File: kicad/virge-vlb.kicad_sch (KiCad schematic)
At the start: 37 parts, among them J2 VGA, U1 86C325, Y1 14.318MHz

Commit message: changed QFP and ROM footprint
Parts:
- J2: footprint Connector_Dsub:DSUB-15-HD_Female_Horizontal_P2.29x1.98mm_EdgePinOffset8.35mm_Housed_MountingHolesOffset10.89mm -> VLB:DSUB-15_female
- U1: footprint Package_QFP:PQFP-208_28x28mm_P0.5mm -> VLB:QFP-208
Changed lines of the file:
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@@
       (effects (font (size 1.524 1.524)) (justify left))
     )
-    (property "Footprint" "Package_QFP:PQFP-208_28x28mm_P0.5mm" (at 201.93 123.19 0)
+    (property "Footprint" "VLB:QFP-208" (at 201.93 123.19 0)
       (effects (font (size 1.524 1.524)) (justify right) hide)
     )
@@
       (effects (font (size 1.27 1.27)))
     )
-    (property "Footprint" "Connector_Dsub:DSUB-15-HD_Female_Horizontal_P2.29x1.98mm_EdgePinOffset8.35mm_Housed_MountingHolesOffset10.89mm" (at 95.25 143.51 0)
+    (property "Footprint" "VLB:DSUB-15_female" (at 95.25 143.51 0)
       (effects (font (size 1.27 1.27)) hide)
     )
@@
       (effects (font (size 1.524 1.524)))
     )
-    (property "Footprint" "Package_QFP:PQFP-208_28x28mm_P0.5mm" (at 149.86 49.53 0)
+    (property "Footprint" "VLB:QFP-208" (at 149.86 49.53 0)
       (effects (font (size 1.524 1.524)) (justify right) hide)
     )

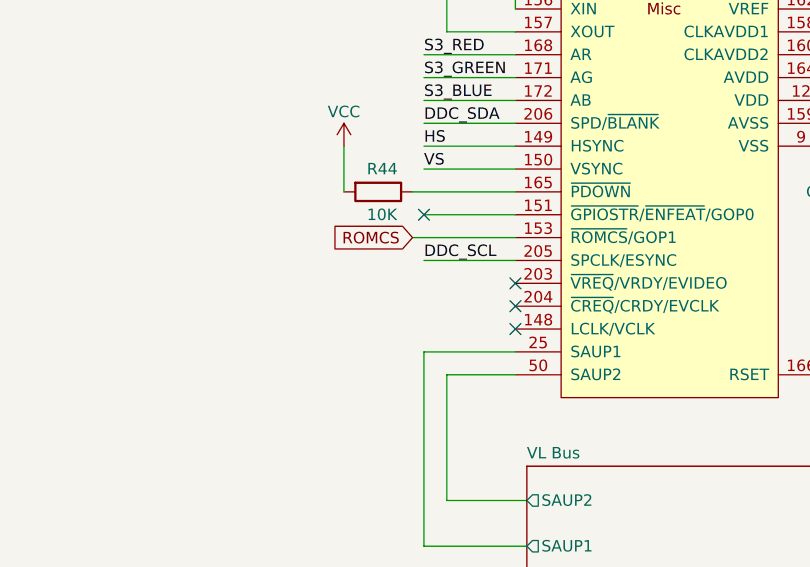
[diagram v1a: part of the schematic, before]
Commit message: added pull up for VREQ
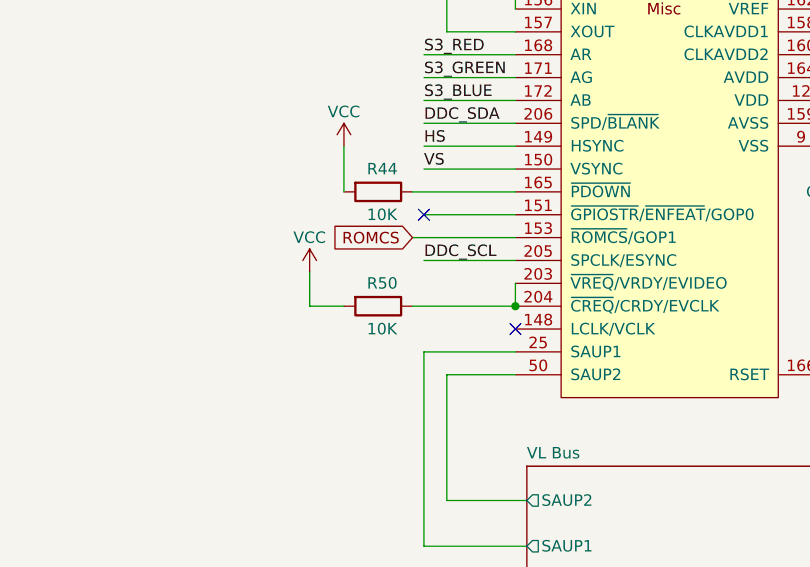
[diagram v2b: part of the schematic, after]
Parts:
- added R50: 10K, Resistor_SMD:R_0805_2012Metric_Pad1.20x1.40mm_HandSolder, symbol Device:R
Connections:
- net VCC: now also R50.2
- net at U1.203 (~{VREQ}/VRDY/EVIDEO): now also U1.204 (~{CREQ}/CRDY/EVCLK), R50.1
- no-connect marks 14 -> 12
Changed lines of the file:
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@@
   (junction (at 219.71 77.47) (diameter 0) (color 0 0 0 0)
+  )
+  (junction (at 173.99 69.85) (diameter 0) (color 0 0 0 0)
   )
   (junction (at 111.76 151.13) (diameter 0) (color 0 0 0 0)
@@
   (no_connect (at 231.14 132.08))
   (no_connect (at 231.14 121.92))
-  (no_connect (at 173.99 69.85))
-  (no_connect (at 173.99 67.31))
   (no_connect (at 231.14 129.54))
   (no_connect (at 63.5 161.29))
@@
     (stroke (width 0) (type default))
   )
+  (wire (pts (xy 173.99 67.31) (xy 173.99 69.85))
+    (stroke (width 0) (type default))
+  )
   (wire (pts (xy 163.83 74.93) (xy 163.83 96.52))
     (stroke (width 0) (type default))
@@
     (stroke (width 0) (type default))
   )
+  (wire (pts (xy 151.13 69.85) (xy 151.13 66.04))
+    (stroke (width 0) (type default))
+  )
   (wire (pts (xy 163.83 44.45) (xy 173.99 44.45))
     (stroke (width 0) (type default))
@@
     (stroke (width 0) (type default))
   )
+  (wire (pts (xy 154.94 69.85) (xy 151.13 69.85))
+    (stroke (width 0) (type default))
+  )
   (wire (pts (xy 111.76 151.13) (xy 111.76 163.83))
     (stroke (width 0) (type default))
@@
   )
   (wire (pts (xy 157.48 27.94) (xy 166.37 27.94))
+    (stroke (width 0) (type default))
+  )
+  (wire (pts (xy 162.56 69.85) (xy 173.99 69.85))
     (stroke (width 0) (type default))
   )
@@
         (path "/e8216711-86b5-4276-82f4-4c7ed22b9a9c"
           (reference "#PWR056") (unit 1)
+        )
+      )
+    )
+  )
+  (symbol (lib_id "power:VCC") (at 151.13 66.04 0) (unit 1)
+    (in_bom yes) (on_board yes) (dnp no) (fields_autoplaced)
+    (property "Reference" "#PWR028" (at 151.13 69.85 0)
+      (effects (font (size 1.27 1.27)) hide)
+    )
+    (property "Value" "VCC" (at 151.13 62.23 0)
+      (effects (font (size 1.27 1.27)))
+    )
+    (property "Footprint" "" (at 151.13 66.04 0)
+      (effects (font (size 1.27 1.27)) hide)
+    )
+    (property "Datasheet" "" (at 151.13 66.04 0)
+      (effects (font (size 1.27 1.27)) hide)
+    )
+    (pin "1")
+    (instances
+      (project "virge-vlb"
+        (path "/e8216711-86b5-4276-82f4-4c7ed22b9a9c"
+          (reference "#PWR028") (unit 1)
         )
       )
@@
         )
       )
+    )
+  )
+  (symbol (lib_id "Device:R") (at 158.75 69.85 270) (unit 1)
+    (in_bom yes) (on_board yes) (dnp no)
+    (property "Reference" "R50" (at 157.48 67.31 90)
+      (effects (font (size 1.27 1.27)) (justify left))
+    )
+    (property "Value" "10K" (at 157.48 72.39 90)
+      (effects (font (size 1.27 1.27)) (justify left))
+    )
+    (property "Footprint" "Resistor_SMD:R_0805_2012Metric_Pad1.20x1.40mm_HandSolder" (at 158.75 68.072 90)
+      (effects (font (size 1.27 1.27)) hide)
+    )
+    (property "Datasheet" "~" (at 158.75 69.85 0)
+      (effects (font (size 1.27 1.27)) hide)
+    )
+    (pin "1")
+    (pin "2")
+    (instances
+      (project "virge-vlb"
+        (path "/e8216711-86b5-4276-82f4-4c7ed22b9a9c"
+          (reference "R50") (unit 1)
+        )
+        (path "/e8216711-86b5-4276-82f4-4c7ed22b9a9c/73bb2a59-bfac-4efc-8051-53849b0f9066"
+          (reference "R16") (unit 1)
+        )
+      )

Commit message: some polishing
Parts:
- removed R43: ADJ, Resistor_SMD:R_0805_2012Metric_Pad1.20x1.40mm_HandSolder, symbol Device:R
- added C26, C27, C28, C29: 10uF, Capacitor_SMD:C_1206_3216Metric_Pad1.33x1.80mm_HandSolder, symbol Device:C_Polarized
- C20, C21, C22, C23, C24, C25: footprint Capacitor_THT:CP_Radial_D5.0mm_P2.50mm -> Capacitor_SMD:C_1206_3216Metric_Pad1.33x1.80mm_HandSolder
- renumbered C17 to C10, C16 to C9, R49 to R11, R10 to R22, R50 to R42, R44 to R43, R42 to R44, R11 to R46
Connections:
- net GND: now also C26.2, C27.2, C28.2, C29.2
- net VCC: now also C26.1, C27.1, C28.1, C29.1

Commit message: some improvements here and there
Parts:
- removed C10, C9: 10pF, Capacitor_SMD:C_0805_2012Metric_Pad1.18x1.45mm_HandSolder, symbol Device:C
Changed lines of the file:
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@@
   (junction (at 208.28 52.07) (diameter 0) (color 0 0 0 0)
   )
-  (junction (at 166.37 27.94) (diameter 0) (color 0 0 0 0)
-  )
   (junction (at 52.07 41.91) (diameter 0) (color 0 0 0 0)
   )
@@
   (junction (at 208.28 39.37) (diameter 0) (color 0 0 0 0)
   )
-  (junction (at 173.99 27.94) (diameter 0) (color 0 0 0 0)
-  )
   (junction (at 127 186.69) (diameter 0) (color 0 0 0 0)
   )
@@
   )
   (junction (at 40.64 41.91) (diameter 0) (color 0 0 0 0)
-  )
-  (junction (at 157.48 20.32) (diameter 0) (color 0 0 0 0)
   )
   (junction (at 48.26 173.99) (diameter 0) (color 0 0 0 0)
@@
     (stroke (width 0) (type default))
   )
-  (wire (pts (xy 151.13 20.32) (xy 151.13 22.86))
-    (stroke (width 0) (type default))
-  )
   (wire (pts (xy 40.64 151.13) (xy 63.5 151.13))
     (stroke (width 0) (type default))
@@
     (stroke (width 0) (type default))
   )
-  (wire (pts (xy 157.48 20.32) (xy 151.13 20.32))
-    (stroke (width 0) (type default))
-  )
   (wire (pts (xy 208.28 44.45) (xy 208.28 46.99))
     (stroke (width 0) (type default))
@@
     (stroke (width 0) (type default))
   )
-  (wire (pts (xy 157.48 20.32) (xy 180.34 20.32))
-    (stroke (width 0) (type default))
-  )
   (wire (pts (xy 33.02 101.6) (xy 54.61 101.6))
     (stroke (width 0) (type default))
@@
     (stroke (width 0) (type default))
   )
-  (wire (pts (xy 173.99 27.94) (xy 180.34 27.94))
-    (stroke (width 0) (type default))
-  )
   (wire (pts (xy 139.7 156.21) (xy 139.7 170.18))
     (stroke (width 0) (type default))
@@
     (stroke (width 0) (type default))
   )
-  (wire (pts (xy 157.48 27.94) (xy 166.37 27.94))
-    (stroke (width 0) (type default))
-  )
   (wire (pts (xy 162.56 69.85) (xy 173.99 69.85))
     (stroke (width 0) (type default))
@@
     (stroke (width 0) (type default))
     (fill (type none))
-  )
-  (text_box "Tune C28,C27 for 14.318Mhz precision"
-    (at 190.5 16.51 0) (size 17.78 7.62)
-    (stroke (width 0) (type default))
-    (fill (type none))
-    (effects (font (size 1.27 1.27)) (justify left top))
   )
   (text_box ""
@@
         (path "/e8216711-86b5-4276-82f4-4c7ed22b9a9c"
           (reference "#PWR028") (unit 1)
-        )
-      )
-    )
-  )
-  (symbol (lib_id "Device:C") (at 157.48 24.13 0) (unit 1)
-    (in_bom yes) (on_board yes) (dnp no)
-    (property "Reference" "C10" (at 160.02 22.86 0)
-      (effects (font (size 1.27 1.27)) (justify left))
-    )
-    (property "Value" "10pF" (at 160.02 26.67 0)
-      (effects (font (size 1.27 1.27)) (justify left))
-    )
-    (property "Footprint" "Capacitor_SMD:C_0805_2012Metric_Pad1.18x1.45mm_HandSolder" (at 158.4452 27.94 0)
-      (effects (font (size 1.27 1.27)) hide)
-    )
-    (property "Datasheet" "~" (at 157.48 24.13 0)
-      (effects (font (size 1.27 1.27)) hide)
-    )
-    (pin "1")
-    (pin "2")
-    (instances
-      (project "virge-vlb"
-        (path "/e8216711-86b5-4276-82f4-4c7ed22b9a9c"
-          (reference "C10") (unit 1)
         )
       )
@@
     )
   )
-  (symbol (lib_id "Device:C") (at 180.34 24.13 0) (unit 1)
-    (in_bom yes) (on_board yes) (dnp no)
-    (property "Reference" "C9" (at 182.88 22.86 0)
-      (effects (font (size 1.27 1.27)) (justify left))
-    )
-    (property "Value" "10pF" (at 182.88 26.67 0)
-      (effects (font (size 1.27 1.27)) (justify left))
-    )
-    (property "Footprint" "Capacitor_SMD:C_0805_2012Metric_Pad1.18x1.45mm_HandSolder" (at 181.3052 27.94 0)
-      (effects (font (size 1.27 1.27)) hide)
-    )
-    (property "Datasheet" "~" (at 180.34 24.13 0)
-      (effects (font (size 1.27 1.27)) hide)
-    )
-    (pin "1")
-    (pin "2")
-    (instances
-      (project "virge-vlb"
-        (path "/e8216711-86b5-4276-82f4-4c7ed22b9a9c"
-          (reference "C9") (unit 1)
-        )
-      )
-    )
-  )
   (symbol (lib_id "Device:C") (at 111.76 167.64 0) (unit 1)
     (in_bom yes) (on_board yes) (dnp no)
@@
         )
       )
-    )
-  )
-  (symbol (lib_id "power:GND") (at 151.13 22.86 0) (unit 1)
-    (in_bom yes) (on_board yes) (dnp no) (fields_autoplaced)
-    (property "Reference" "#PWR058" (at 151.13 29.21 0)
-      (effects (font (size 1.27 1.27)) hide)
-    )
-    (property "Value" "GND" (at 151.13 27.94 0)
-      (effects (font (size 1.27 1.27)))
-    )
-    (property "Footprint" "" (at 151.13 22.86 0)
-      (effects (font (size 1.27 1.27)) hide)
-    )
-    (property "Datasheet" "" (at 151.13 22.86 0)
-      (effects (font (size 1.27 1.27)) hide)
-    )
-    (pin "1")
-    (instances
-      (project "virge-vlb"
-        (path "/e8216711-86b5-4276-82f4-4c7ed22b9a9c"
-          (reference "#PWR058") (unit 1)
-        )
-      )

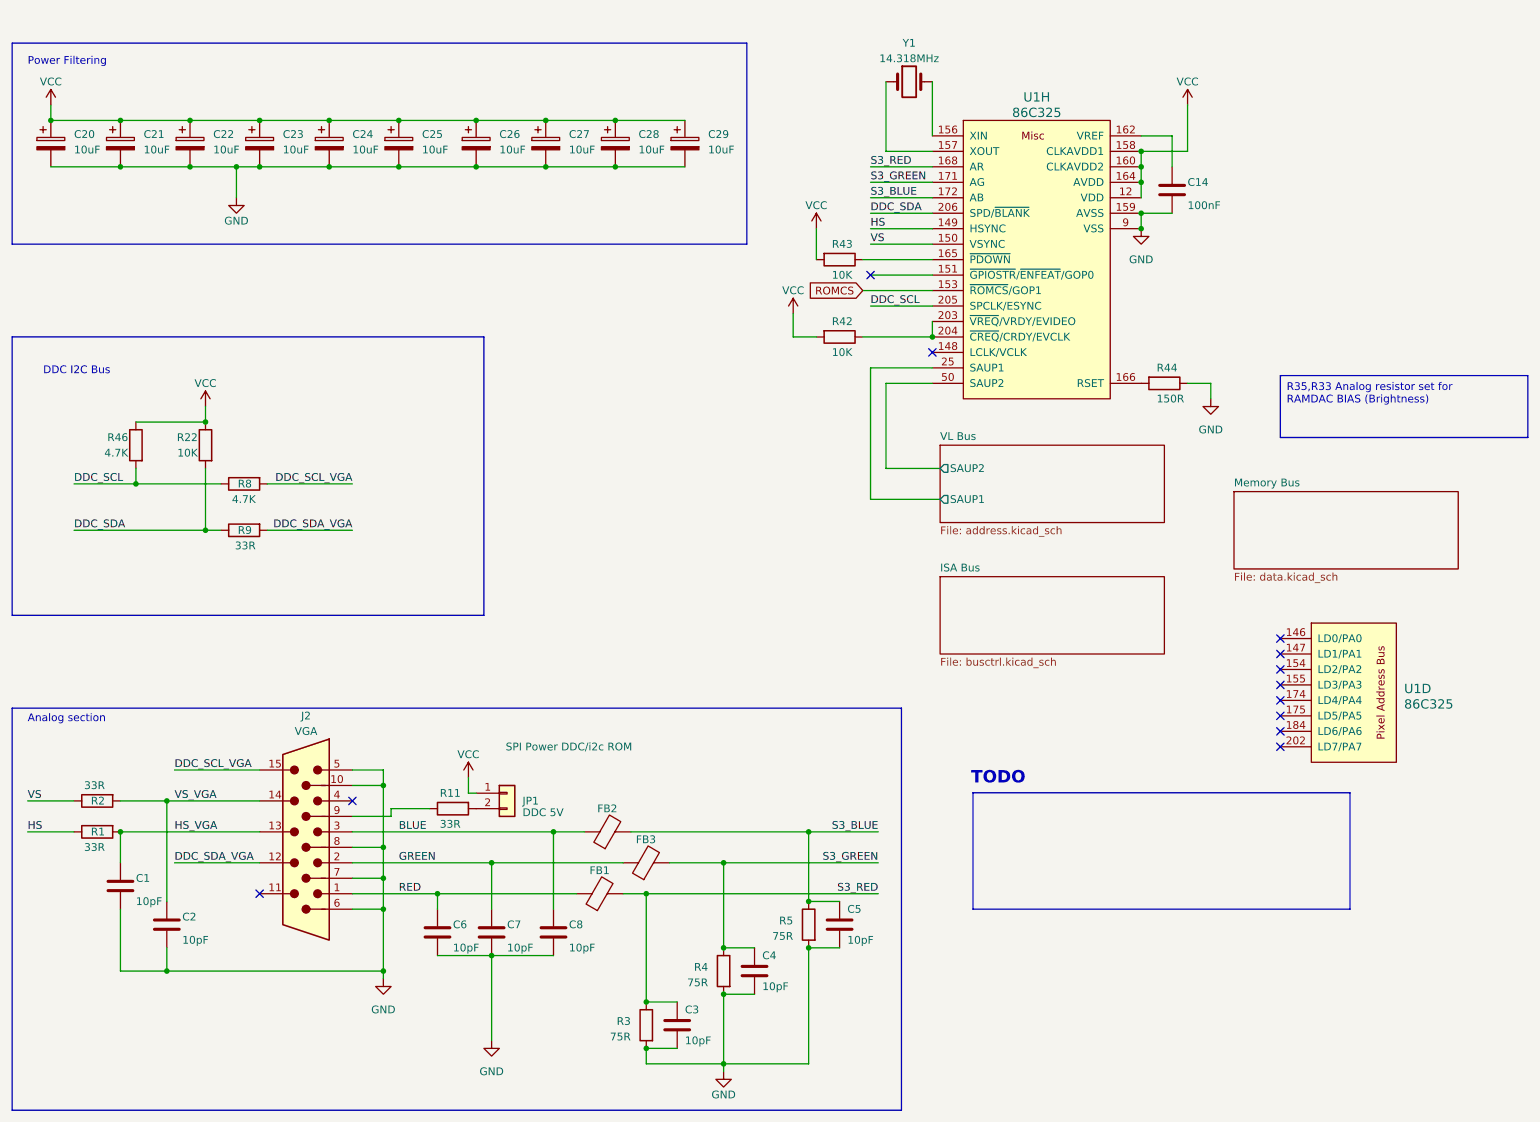
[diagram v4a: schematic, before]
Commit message: some optimizations and silkscreen updating
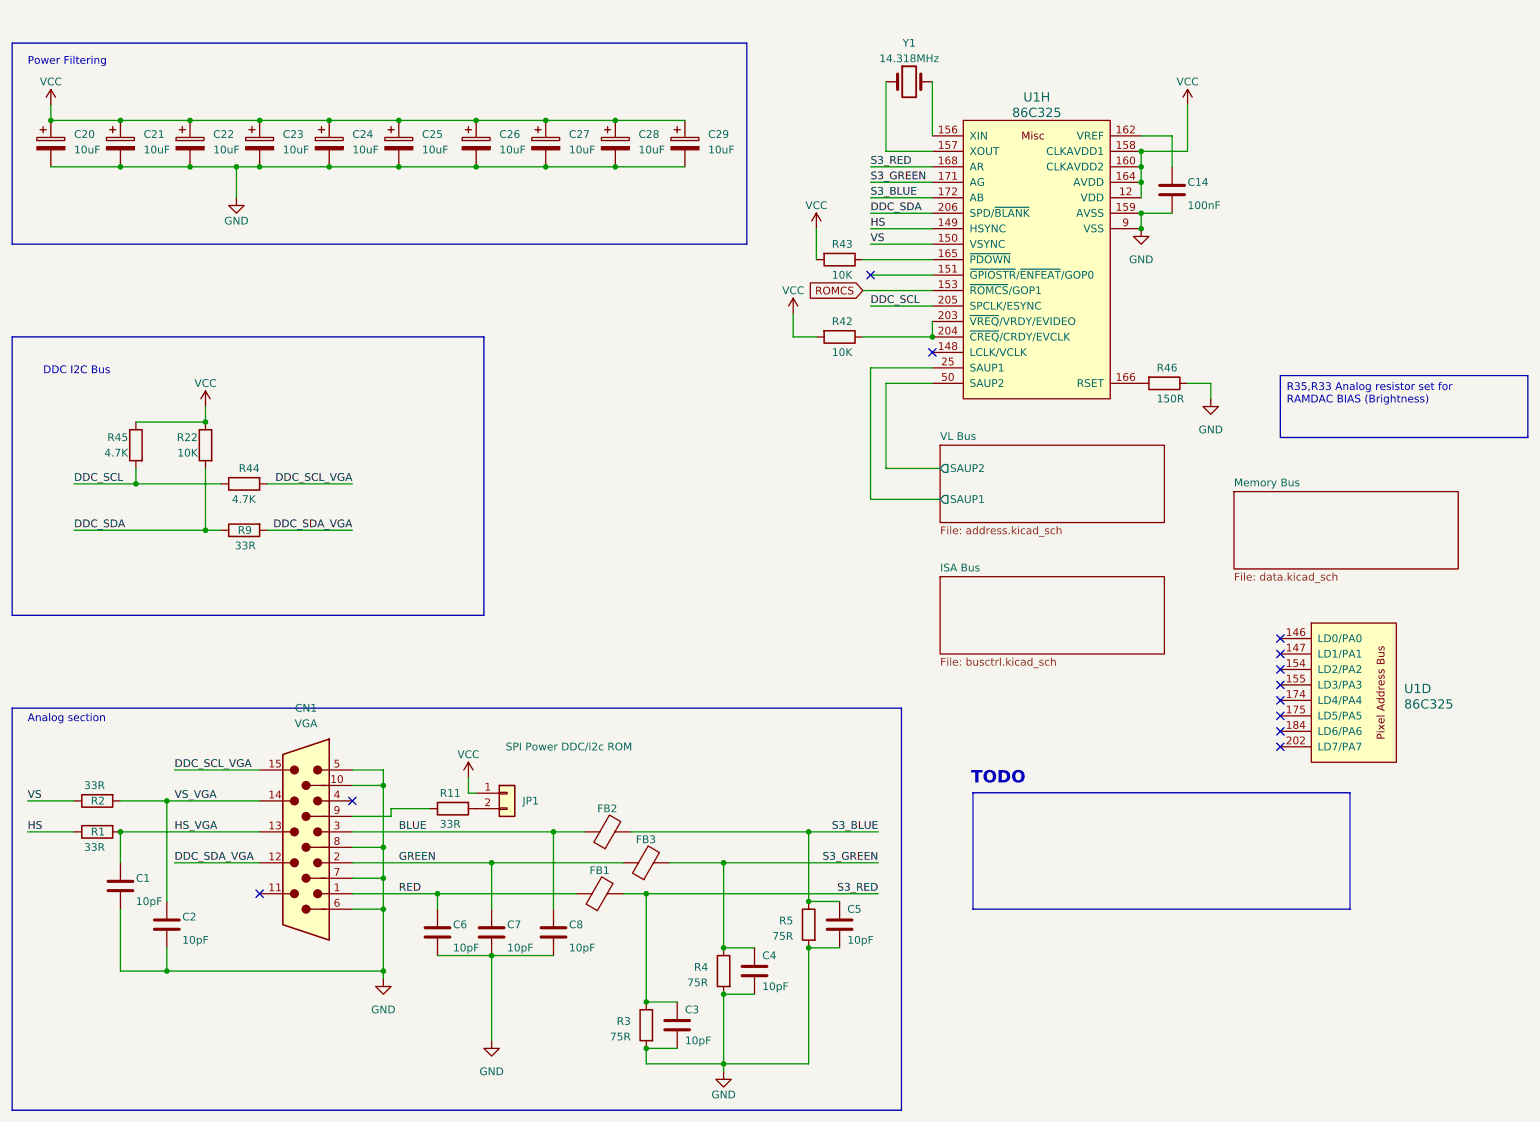
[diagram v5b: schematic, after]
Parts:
- JP1: value DDC 5V -> Conn_01x02
- renumbered J2 to CN1, R8 to R44, R46 to R45, R44 to R46
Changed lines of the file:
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@@
       (effects (font (size 1.27 1.27)) (justify left))
     )
-    (property "Value" "DDC 5V" (at 106.68 147.955 0)
-      (effects (font (size 1.27 1.27)) (justify left))
+    (property "Value" "Conn_01x02" (at 106.68 147.955 0)
+      (effects (font (size 1.27 1.27)) (justify left) hide)
     )
     (property "Footprint" "Connector_PinHeader_2.54mm:PinHeader_1x02_P2.54mm_Vertical" (at 104.14 144.78 0)
@@
   (symbol (lib_id "Device:R") (at 60.96 93.98 90) (mirror x) (unit 1)
     (in_bom yes) (on_board yes) (dnp no)
-    (property "Reference" "R8" (at 62.23 93.98 90)
+    (property "Reference" "R44" (at 63.5 91.44 90)
       (effects (font (size 1.27 1.27)) (justify left))
     )
@@
       (project "virge-vlb"
         (path "/e8216711-86b5-4276-82f4-4c7ed22b9a9c"
-          (reference "R8") (unit 1)
+          (reference "R44") (unit 1)
         )
       )
@@
   (symbol (lib_id "Connector:DE15_Plug_HighDensity") (at 71.12 153.67 0) (mirror y) (unit 1)
     (in_bom yes) (on_board yes) (dnp no) (fields_autoplaced)
-    (property "Reference" "J2" (at 71.12 132.08 0)
-      (effects (font (size 1.27 1.27)))
-    )
-    (property "Value" "VGA" (at 71.12 134.62 0)
+    (property "Reference" "CN1" (at 71.12 130.81 0)
+      (effects (font (size 1.27 1.27)))
+    )
+    (property "Value" "VGA" (at 71.12 133.35 0)
       (effects (font (size 1.27 1.27)))
     )
@@
       (project "virge-vlb"
         (path "/e8216711-86b5-4276-82f4-4c7ed22b9a9c"
-          (reference "J2") (unit 1)
+          (reference "CN1") (unit 1)
         )
       )
@@
   (symbol (lib_id "Device:R") (at 212.09 77.47 270) (unit 1)
     (in_bom yes) (on_board yes) (dnp no)
-    (property "Reference" "R44" (at 210.82 74.93 90)
+    (property "Reference" "R46" (at 210.82 74.93 90)
       (effects (font (size 1.27 1.27)) (justify left))
     )
@@
       (project "virge-vlb"
         (path "/e8216711-86b5-4276-82f4-4c7ed22b9a9c"
-          (reference "R44") (unit 1)
+          (reference "R46") (unit 1)
         )
         (path "/e8216711-86b5-4276-82f4-4c7ed22b9a9c/73bb2a59-bfac-4efc-8051-53849b0f9066"
@@
   (symbol (lib_id "Device:R") (at 43.18 87.63 0) (mirror y) (unit 1)
     (in_bom yes) (on_board yes) (dnp no)
-    (property "Reference" "R46" (at 41.91 86.36 0)
+    (property "Reference" "R45" (at 41.91 86.36 0)
       (effects (font (size 1.27 1.27)) (justify left))
     )
@@
       (project "virge-vlb"
         (path "/e8216711-86b5-4276-82f4-4c7ed22b9a9c"
-          (reference "R46") (unit 1)
-        )
-      )
+          (reference "R45") (unit 1)
+        )
+      )
